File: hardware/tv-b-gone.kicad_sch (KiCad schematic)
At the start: 13 parts, among them Q1 2N7000, SW1 SW_Push, U1 ATtiny85-20P

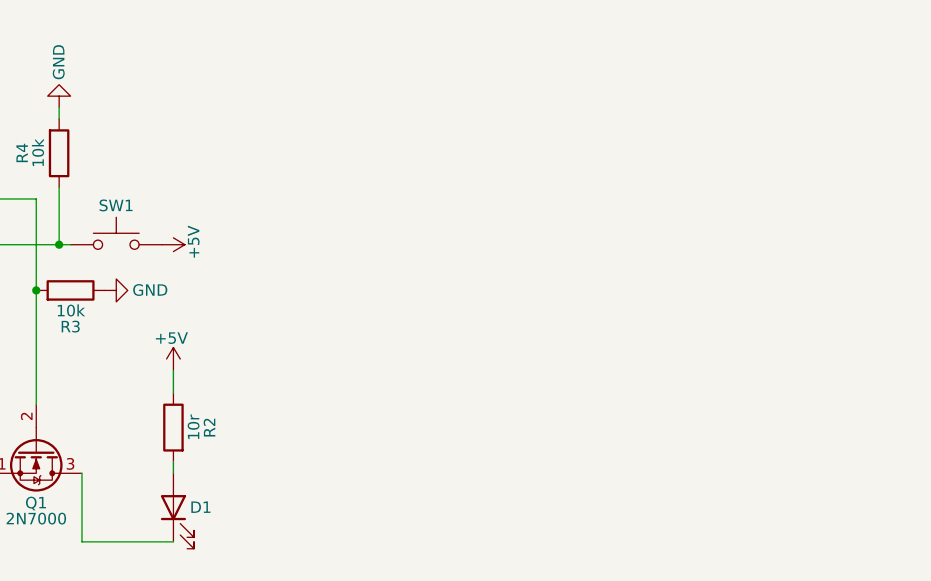
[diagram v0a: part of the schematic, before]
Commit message: Added a USB-C power receptacle and fixed design rules
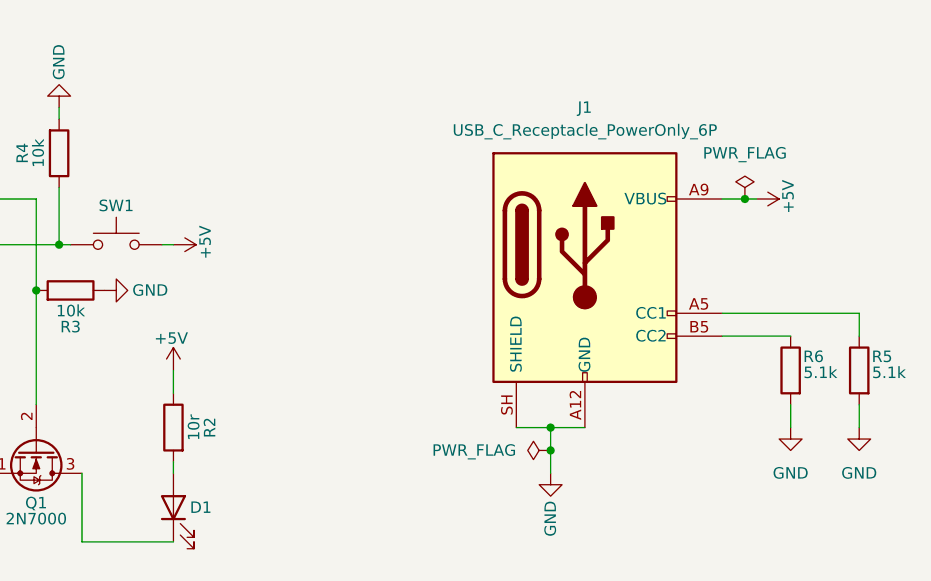
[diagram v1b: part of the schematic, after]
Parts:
- added J1: USB_C_Receptacle_PowerOnly_6P, symbol Connector:USB_C_Receptacle_PowerOnly_6P
- added R5, R6: 5.1k, Resistor_SMD:R_0805_2012Metric, symbol Device:R
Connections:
- net +5V: now also J1.A9 (VBUS), J1.B9 (VBUS)
- net GND: now also J1.A12 (GND), J1.B12 (GND), J1.SH (SHIELD), R5.2, R6.2
- new net: J1.B5 (CC2), R6.1
- new net: J1.A5 (CC1), R5.1

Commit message: Added status LED
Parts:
- added D2: LED, LED_THT:LED_D3.0mm, symbol Device:LED
- added R7: 220r, Resistor_SMD:R_0805_2012Metric, symbol Device:R
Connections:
- net GND: now also D2.1 (K)
- net at U1.2 (XTAL1/PB3): now also R7.2
- new net: D2.2 (A), R7.1
- no-connect marks 2 -> 1

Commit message: Added test points for GND and VCC
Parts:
- added TP_GND1, TP_VCC1: TestPoint, TestPoint:TestPoint_Pad_D2.0mm, symbol Connector:TestPoint
- J1: footprint (none) -> Connector_USB:USB_C_Receptacle_XKB_U262-16XN-4BVC11
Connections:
- net +5V: now also TP_VCC1.1
- net GND: now also TP_GND1.1

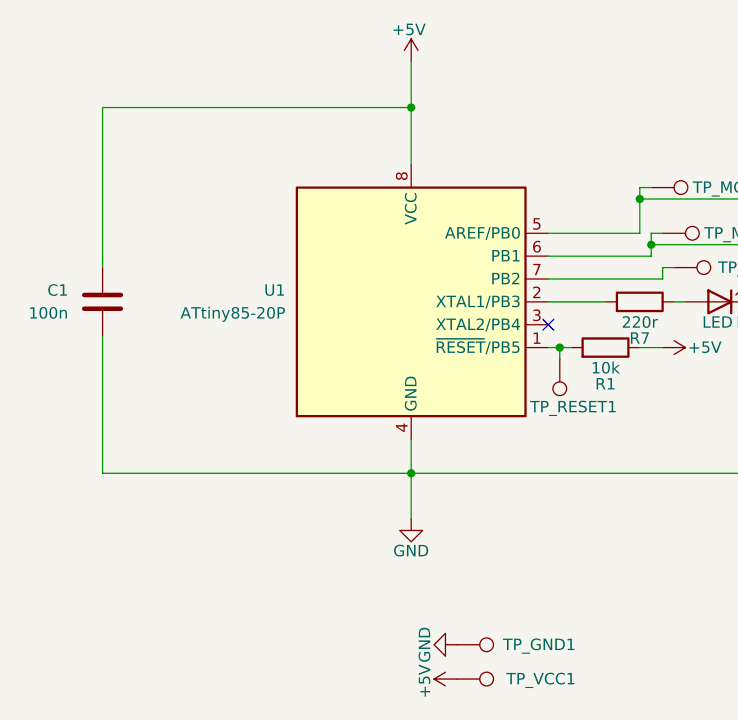
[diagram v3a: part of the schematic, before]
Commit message: PCB power test points connected
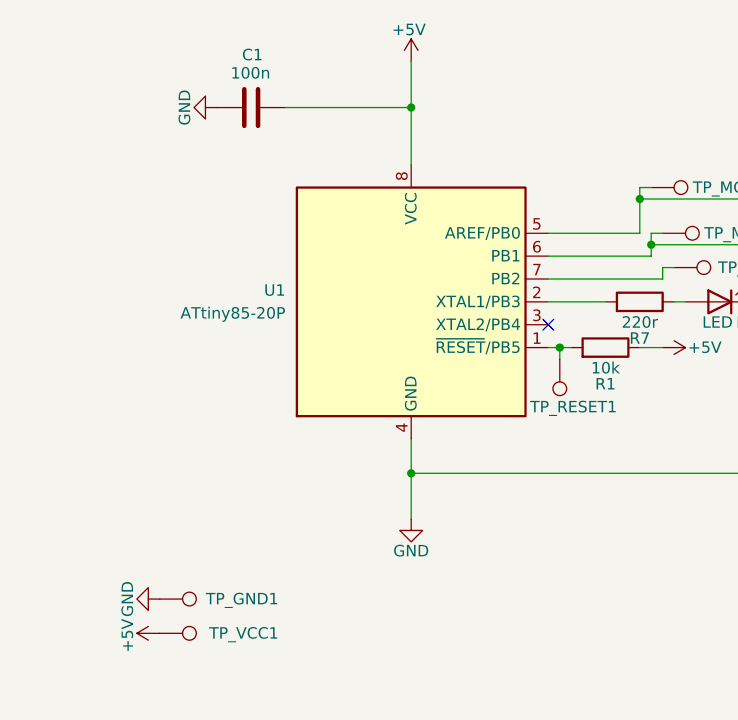
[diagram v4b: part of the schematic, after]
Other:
- moved on the sheet: C1, TP_GND1, TP_VCC1
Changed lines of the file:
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@@
+	(wire
+		(pts
+			(xy 74.93 40.64) (xy 74.93 46.99)
+		)
+		(stroke
+			(width 0)
+			(type default)
+		)
+	)
 	(wire
 		(pts
@@
 	(wire
 		(pts
-			(xy 74.93 40.64) (xy 74.93 46.99)
+			(xy 74.93 35.56) (xy 74.93 40.64)
 		)
 		(stroke
@@
 	(wire
 		(pts
-			(xy 40.64 40.64) (xy 74.93 40.64)
-		)
-		(stroke
-			(width 0)
-			(type default)
-		)
-	)
-	(wire
-		(pts
 			(xy 101.6 54.61) (xy 101.6 55.88)
 		)
@@
 	(wire
 		(pts
-			(xy 40.64 81.28) (xy 40.64 66.04)
-		)
-		(stroke
-			(width 0)
-			(type default)
-		)
-	)
-	(wire
-		(pts
 			(xy 74.93 81.28) (xy 74.93 77.47)
 		)
@@
 	(wire
 		(pts
-			(xy 74.93 81.28) (xy 40.64 81.28)
-		)
-		(stroke
-			(width 0)
-			(type default)
-		)
-	)
-	(wire
-		(pts
 			(xy 90.17 67.31) (xy 91.44 67.31)
 		)
@@
 	(wire
 		(pts
-			(xy 40.64 58.42) (xy 40.64 40.64)
-		)
-		(stroke
-			(width 0)
-			(type default)
-		)
-	)
-	(wire
-		(pts
-			(xy 74.93 35.56) (xy 74.93 40.64)
-		)
-		(stroke
-			(width 0)
-			(type default)
-		)
-	)
-	(wire
-		(pts
 			(xy 121.92 60.96) (xy 121.92 73.66)
 		)
@@
 		(pts
 			(xy 179.07 78.74) (xy 179.07 81.28)
+		)
+		(stroke
+			(width 0)
+			(type default)
+		)
+	)
+	(wire
+		(pts
+			(xy 60.96 40.64) (xy 74.93 40.64)
 		)
 		(stroke
@@
 	(symbol
 		(lib_id "Connector:TestPoint")
-		(at 80.01 104.14 270)
+		(at 46.99 99.06 270)
 		(unit 1)
 		(body_style 1)
@@
 		(dnp no)
 		(property "Reference" "TP_VCC1"
-			(at 93.218 104.14 90)
+			(at 60.198 99.06 90)
 			(show_name no)
 			(do_not_autoplace no)
@@
 		)
 		(property "Value" "TestPoint"
-			(at 84.5819 101.6 0)
+			(at 51.5619 96.52 0)
 			(hide yes)
 			(show_name no)
@@
 		)
 		(property "Footprint" "TestPoint:TestPoint_Pad_D2.0mm"
-			(at 80.01 109.22 0)
+			(at 46.99 104.14 0)
 			(hide yes)
 			(show_name no)
@@
 		)
 		(property "Datasheet" ""
-			(at 80.01 109.22 0)
+			(at 46.99 104.14 0)
 			(hide yes)
 			(show_name no)
@@
 		)
 		(property "Description" "test point"
-			(at 80.01 104.14 0)
+			(at 46.99 99.06 0)
 			(hide yes)
 			(show_name no)
@@
 	(symbol
 		(lib_id "power:GND")
+		(at 53.34 40.64 270)
+		(unit 1)
+		(body_style 1)
+		(exclude_from_sim no)
+		(in_bom yes)
+		(on_board yes)
+		(in_pos_files yes)
+		(dnp no)
+		(property "Reference" "#PWR015"
+			(at 46.99 40.64 0)
+			(hide yes)
+			(show_name no)
+			(do_not_autoplace no)
+			(effects
+				(font
+					(size 1.27 1.27)
+				)
+			)
+		)
+		(property "Value" "GND"
+			(at 49.784 40.64 0)
+			(show_name no)
+			(do_not_autoplace no)
+			(effects
+				(font
+					(size 1.27 1.27)
+				)
+			)
+		)
+		(property "Footprint" ""
+			(at 53.34 40.64 0)
+			(hide yes)
+			(show_name no)
+			(do_not_autoplace no)
+			(effects
+				(font
+					(size 1.27 1.27)
+				)
+			)
+		)
+		(property "Datasheet" ""
+			(at 53.34 40.64 0)
+			(hide yes)
+			(show_name no)
+			(do_not_autoplace no)
+			(effects
+				(font
+					(size 1.27 1.27)
+				)
+			)
+		)
+		(property "Description" "Power symbol creates a global label with name \"GND\" , ground"
+			(at 53.34 40.64 0)
+			(hide yes)
+			(show_name no)
+			(do_not_autoplace no)
+			(effects
+				(font
+					(size 1.27 1.27)
+				)
+			)
+		)
+		(pin "1"
+		)
+		(instances
+			(project "tv-b-gone"
+				(path "/23a371e7-c0c2-4fe5-805f-b61be48edc46"
+					(reference "#PWR015")
+					(unit 1)
+				)
+			)
+		)
+	)
+	(symbol
+		(lib_id "power:GND")
 		(at 179.07 81.28 0)
 		(unit 1)
@@
 	(symbol
 		(lib_id "power:GND")
-		(at 80.01 100.33 270)
+		(at 46.99 95.25 270)
 		(unit 1)
 		(body_style 1)
@@
 		(dnp no)
 		(property "Reference" "#PWR013"
-			(at 73.66 100.33 0)
+			(at 40.64 95.25 0)
 			(hide yes)
 			(show_name no)
@@
 		)
 		(property "Value" "GND"
-			(at 76.454 100.33 0)
+			(at 43.434 95.25 0)
 			(show_name no)
 			(do_not_autoplace no)
@@
 		)
 		(property "Footprint" ""
-			(at 80.01 100.33 0)
+			(at 46.99 95.25 0)
 			(hide yes)
 			(show_name no)
@@
 		)
 		(property "Datasheet" ""
-			(at 80.01 100.33 0)
+			(at 46.99 95.25 0)
 			(hide yes)
 			(show_name no)
@@
 		)
 		(property "Description" "Power symbol creates a global label with name \"GND\" , ground"
-			(at 80.01 100.33 0)
+			(at 46.99 95.25 0)
 			(hide yes)
 			(show_name no)
@@
 	(symbol
 		(lib_id "power:+5V")
-		(at 80.01 104.14 90)
+		(at 46.99 99.06 90)
 		(unit 1)
 		(body_style 1)
@@
 		(dnp no)
 		(property "Reference" "#PWR014"
-			(at 83.82 104.14 0)
+			(at 50.8 99.06 0)
 			(hide yes)
 			(show_name no)
@@
 		)
 		(property "Value" "+5V"
-			(at 76.454 104.394 0)
+			(at 43.434 99.314 0)
 			(show_name no)
 			(do_not_autoplace no)
@@
 		)
 		(property "Footprint" ""
-			(at 80.01 104.14 0)
+			(at 46.99 99.06 0)
 			(hide yes)
 			(show_name no)
@@
 		)
 		(property "Datasheet" ""
-			(at 80.01 104.14 0)
+			(at 46.99 99.06 0)
 			(hide yes)
 			(show_name no)
@@
 		)
 		(property "Description" "Power symbol creates a global label with name \"+5V\""
-			(at 80.01 104.14 0)
+			(at 46.99 99.06 0)
 			(hide yes)
 			(show_name no)
@@
 	(symbol
 		(lib_id "Device:C")
-		(at 40.64 62.23 0)
+		(at 57.15 40.64 90)
 		(mirror x)
 		(unit 1)
@@
 		(dnp no)
 		(property "Reference" "C1"
-			(at 36.83 60.9599 0)
+			(at 56.134 34.798 90)
 			(show_name no)
 			(do_not_autoplace no)
@@
 		)
 		(property "Value" "100n"
-			(at 36.83 63.4999 0)
+			(at 54.864 36.83 90)
 			(show_name no)
 			(do_not_autoplace no)
@@
 		)
 		(property "Footprint" "Capacitor_SMD:C_0805_2012Metric"
-			(at 41.6052 58.42 0)
+			(at 60.96 41.6052 0)
 			(hide yes)
 			(show_name no)
@@
 		)
 		(property "Datasheet" ""
-			(at 40.64 62.23 0)
+			(at 57.15 40.64 0)
 			(hide yes)
 			(show_name no)
@@
 		)
 		(property "Description" "Unpolarized capacitor"
-			(at 40.64 62.23 0)
+			(at 57.15 40.64 0)
 			(hide yes)
 			(show_name no)
@@
 	(symbol
 		(lib_id "Connector:TestPoint")
-		(at 80.01 100.33 270)
+		(at 46.99 95.25 270)
 		(unit 1)
 		(body_style 1)
@@
 		(dnp no)
 		(property "Reference" "TP_GND1"
-			(at 93.218 100.33 90)
+			(at 60.198 95.25 90)
 			(show_name no)
 			(do_not_autoplace no)
@@
 		)
 		(property "Value" "TestPoint"
-			(at 84.5819 97.79 0)
+			(at 51.5619 92.71 0)
 			(hide yes)
 			(show_name no)
@@
 		)
 		(property "Footprint" "TestPoint:TestPoint_Pad_D2.0mm"
-			(at 80.01 105.41 0)
+			(at 46.99 100.33 0)
 			(hide yes)
 			(show_name no)
@@
 		)
 		(property "Datasheet" ""
-			(at 80.01 105.41 0)
+			(at 46.99 100.33 0)
 			(hide yes)
 			(show_name no)
@@
 		)
 		(property "Description" "test point"
-			(at 80.01 100.33 0)
-			(hide yes)
-			(show_name no)
+			(at 46.99 95.25 0)
+			(hide yes)
+			(show_name no)

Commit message: PCB finished
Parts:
- J1: footprint Connector_USB:USB_C_Receptacle_XKB_U262-16XN-4BVC11 -> Connector_USB:USB_C_Receptacle_GCT_USB4125-xx-x-0190_6P_TopMnt_Horizontal
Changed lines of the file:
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@@
 	(wire
 		(pts
-			(xy 74.93 35.56) (xy 74.93 40.64)
+			(xy 74.93 30.48) (xy 74.93 40.64)
 		)
 		(stroke
@@
 	(symbol
 		(lib_id "power:+5V")
-		(at 74.93 35.56 0)
+		(at 74.93 30.48 0)
 		(unit 1)
 		(body_style 1)
@@
 		(dnp no)
 		(property "Reference" "#PWR03"
-			(at 74.93 39.37 0)
+			(at 74.93 34.29 0)
 			(hide yes)
 			(show_name no)
@@
 		)
 		(property "Value" "+5V"
-			(at 74.676 32.004 0)
+			(at 74.676 26.924 0)
 			(show_name no)
 			(do_not_autoplace no)
@@
 		)
 		(property "Footprint" ""
-			(at 74.93 35.56 0)
-			(hide yes)
-			(show_name no)
-			(do_not_autoplace no)
-			(effects
-				(font
-					(size 1.27 1.27)
-				)
-			)
-		)
-		(property "Datasheet" ""
-			(at 74.93 35.56 0)
+			(at 74.93 30.48 0)
+			(hide yes)
+			(show_name no)
+			(do_not_autoplace no)
+			(effects
+				(font
+					(size 1.27 1.27)
+				)
+			)
+		)
+		(property "Datasheet" ""
+			(at 74.93 30.48 0)
 			(hide yes)
 			(show_name no)
@@
 		)
 		(property "Description" "Power symbol creates a global label with name \"+5V\""
-			(at 74.93 35.56 0)
+			(at 74.93 30.48 0)
 			(hide yes)
 			(show_name no)
@@
 			)
 		)
-		(property "Footprint" "Connector_USB:USB_C_Receptacle_XKB_U262-16XN-4BVC11"
+		(property "Footprint" "Connector_USB:USB_C_Receptacle_GCT_USB4125-xx-x-0190_6P_TopMnt_Horizontal"
 			(at 186.69 55.88 0)
 			(hide yes)
